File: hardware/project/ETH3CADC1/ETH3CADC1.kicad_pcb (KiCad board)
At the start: 2 copper layers, 73 x 100 mm, 235 parts, among them J1101 Conn_02x10_Odd_Even, J1201 Conn_02x10_Odd_Even, J1301 Conn_02x05_Odd_Even, J401 20021111-00010T4LF, J402 Conn_02x01, J701 Conn_02x10_Odd_Even, J801 Conn_02x02_Odd_Even, J802 Conn_02x04_Odd_Even, Q301 MMBTA55, Q302 BC847, U1001 LM337_SOT223, U1301 AP2127K-1.2, U1302 ICE40UP5K-SG48ITR, U1303 W25Q32JVSS, U201 DG211, U202 DG211B, U203 OPA2192, U204 DG419DY, U205 OPA140, U206 LT5400-100k-100k, U207 LT5400-5k-1k, U208 OPA177, U209 OPA140, U210 LT5400-10k-10k, U211 OPA192, U212 LM311, U301 LT1021-7, U302 LM399H, U303 OPA177, U401 HDC1080, U402 MCP2551-I-SN, U403 STM32H743ZI, U404 PCA9517, U405 24LC08B-E/MS, U501 LAN8742A, U502 LC03-3.3, U503 LC03-3.3, U601 TXB0104PW, U602 ADuM5402, U603 74AC125, U901 MT48LC16M16A2P-6A, X1301 ASAAIG-40.000MHZ, Y401 NX3225GD-8MHZ, Y501 NX5032GA-25.000M-LN-CD-1

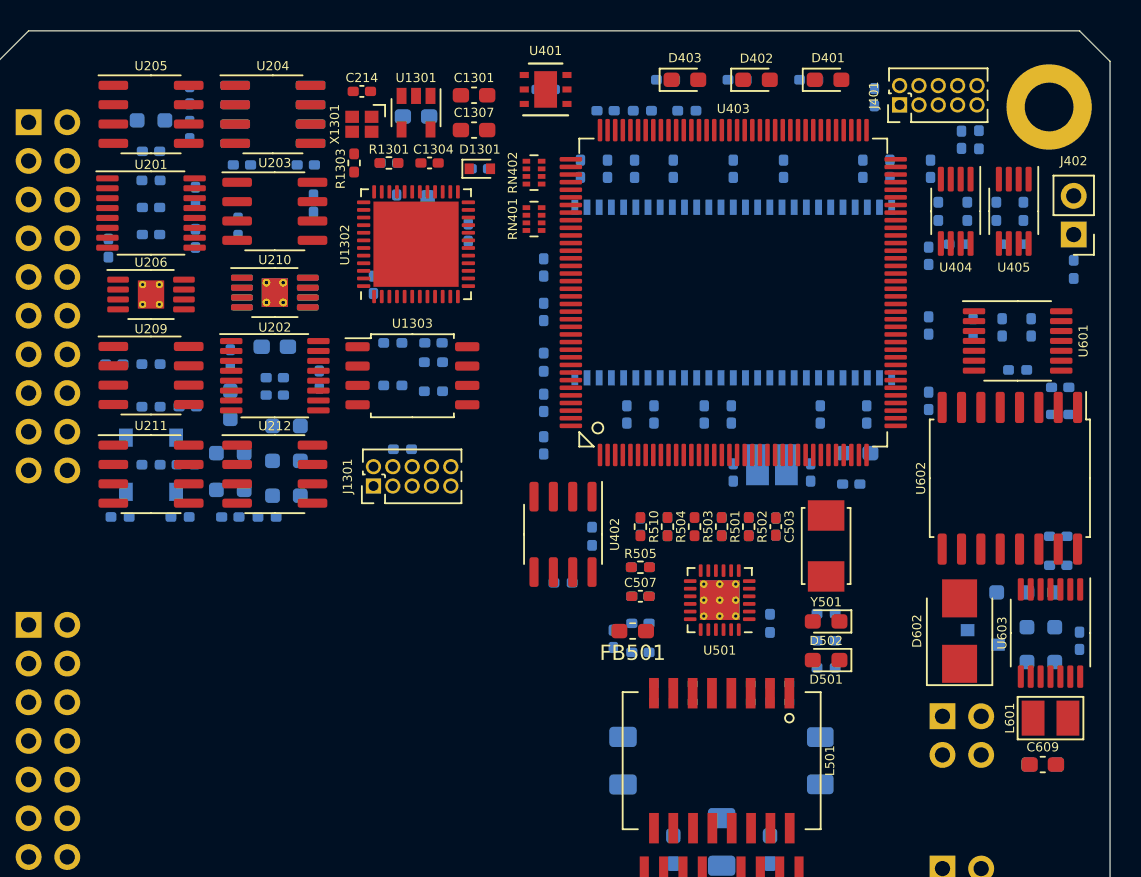
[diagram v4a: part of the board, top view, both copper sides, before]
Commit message: Added SDRAM to the linker file.
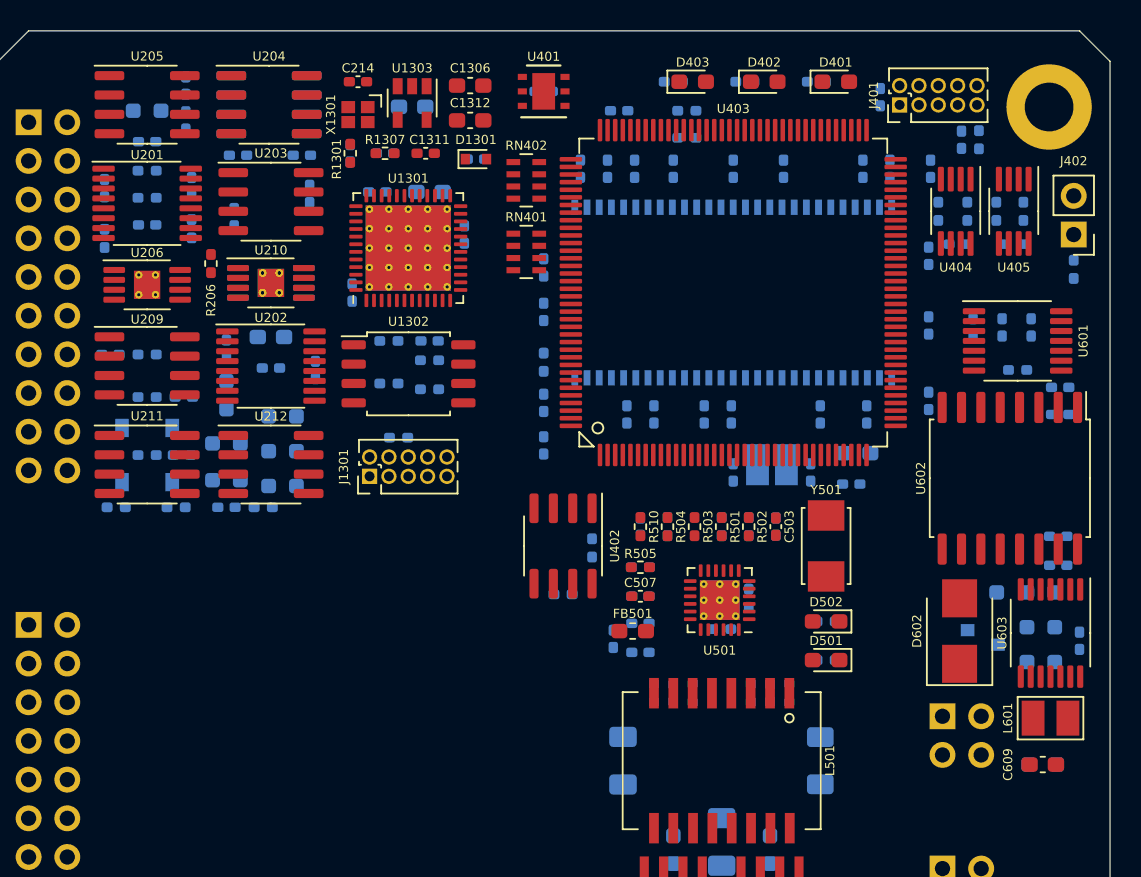
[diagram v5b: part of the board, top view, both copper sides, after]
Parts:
- removed the R203 at (161.0, 59.8)
- added R201: 10k, Resistor_SMD:R_0402_1005Metric_Pad0.72x0.64mm_HandSolder, B.Cu at (160.8, 61.0)
- added R204: 10k, Resistor_SMD:R_0402_1005Metric_Pad0.72x0.64mm_HandSolder, B.Cu at (160.8, 59.2)
- added R206: 10k, Resistor_SMD:R_0402_1005Metric_Pad0.72x0.64mm_HandSolder, F.Cu at (165.0, 65.3)
- D501: value GREEN -> YELLOW
- D502: value YELLOW -> GREEN
- RN401, RN402: footprint Resistor_SMD:R_Array_Concave_4x0402 -> Resistor_SMD:R_Array_Concave_4x0603
- U1301: renamed from U1302; footprint Package_DFN_QFN:QFN-48-1EP_7x7mm_P0.5mm_EP5.6x5.6mm -> Package_DFN_QFN:QFN-48-1EP_7x7mm_P0.5mm_EP5.6x5.6mm_ThermalVias
- moved C218 14.1 mm to (174.1, 58.0), turned to 270 degrees
- moved C219 14.0 mm to (160.8, 62.7)
- moved R511 6.83 mm to (200.3, 87.2), turned to 90 degrees
- moved R402 3.42 mm to (196.2, 57.0), turned to 180 degrees
- moved C210 3.30 mm to (158.0, 60.3), turned to 90 degrees
- moved R512 3.20 mm to (198.5, 89.3), turned to 0 degrees
- moved RN401 2.22 mm to (185.7, 64.5)
- moved C1303 1.49 mm to (174.2, 67.2)
- moved C1302 1.48 mm to (175.9, 60.6), turned to 180 degrees
- moved C1310 1.28 mm to (179.3, 60.6), turned to 0 degrees
- moved R513 1.27 mm to (205.4, 91.3)
- moved C405 0.89 mm to (191.8, 55.2)
- moved R1302 0.80 mm to (177.3, 76.7)
- moved R401 0.76 mm to (188.1, 87.0)
- moved R403 0.76 mm to (190.0, 83.9)
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- renumbered C1308 to C1301, C1309 to C1302, C1310 to C1303, C1311 to C1304, C1312 to C1305, C1301 to C1306, C1302 to C1307, C1303 to C1308, C1305 to C1309, C1306 to C1310, C1304 to C1311, C1307 to C1312, R1303 to R1301, R1305 to R1302, R1302 to R1303, R1306 to R1305, R1307 to R1306, R1301 to R1307, R201 to R202, R202 to R203, R204 to R205, R205 to R207, R206 to R208, R207 to R209, R208 to R210, R209 to R211, R210 to R212, R211 to R213, R212 to R214, R213 to R215, R214 to R216, R215 to R217, R216 to R218, U1303 to U1302, U1301 to U1303
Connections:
- net /ADC 1/FPGA1_MUX_10V renamed /ADC 1/FPGA1_MUX_P10V
- net /ADC 1/VREF1_-7V renamed Net-(U204-Pad8)
- C1301 pad 1: +3V3 -> +3.3VF
- C1302 pad 1: +3V3 -> +3.3VF
- C1303 pad 1: +3V3 -> +3.3VF
- C1304 pad 1: +3V3 -> +3.3VF
- C1305 pad 1: +3V3 -> +3.3VF
- C1306 pad 1: +3V3 -> +3.3VF
- C1309 pad 1: +3V3 -> +3.3VF
- C218 pad 1: +5VF -> +3.3VF
- C218 pad 2: DGNDF -> AGNDF
- C219 pad 1: +5VF -> +3.3VF
- C219 pad 2: DGNDF -> AGNDF
- C220 pad 1: +3.3VP -> +3.3VF
- C301 pad 1: /VREF/VREF_N7V_LPF -> /ADC 1/VREF_N7V_LPF
- C401 pad 1: +3V3 -> +3.3VF
- C402 pad 1: +3V3 -> +3.3VF
- C403 pad 1: +3V3 -> +3.3VF
- C404 pad 1: +3V3 -> +3.3VF
- C405 pad 1: +3V3 -> +3.3VF
- C406 pad 1: +3V3 -> +3.3VF
- C407 pad 1: +3V3 -> +3.3VF
- C408 pad 1: +3V3 -> +3.3VF
- C409 pad 1: +3V3 -> +3.3VF
- C410 pad 1: +3V3 -> +3.3VF
- C411 pad 1: +3V3 -> +3.3VF
- C412 pad 1: +3V3 -> +3.3VF
- C413 pad 1: +3V3 -> +3.3VF
- C417 pad 1: +3V3 -> +3.3VF
- C420 pad 1: +3V3 -> +3.3VF
- C421 pad 1: +3V3 -> +3.3VF
- C422 pad 1: +3V3 -> +3.3VF
- C423 pad 1: +3V3 -> +3.3VF
- C502 pad 1: +3V3 -> +3.3VF
- C505 pad 1: +3V3 -> +3.3VF
- C601 pad 1: +3V3 -> +3.3VF
- C602 pad 1: +3V3 -> +3.3VF
- C901 pad 1: +3V3 -> +3.3VF
- C902 pad 1: +3V3 -> +3.3VF
- C903 pad 1: +3V3 -> +3.3VF
- C904 pad 1: +3V3 -> +3.3VF
- C905 pad 1: +3V3 -> +3.3VF
- C906 pad 1: +3V3 -> +3.3VF
- C907 pad 1: +3V3 -> +3.3VF
- D1301 pad 2: +3V3 -> +3.3VF
- D401 pad 2: +3V3 -> +3.3VF
- D402 pad 2: +3V3 -> +3.3VF
- D403 pad 2: +3V3 -> +3.3VF
- FB401 pad 2: +3V3 -> +3.3VF
- FB501 pad 2: +3V3 -> +3.3VF
- J1101 pad 15: +3V3 -> +3.3VF
- J1101 pad 16: +3V3 -> +3.3VF
- J1201 pad 15: +3V3 -> +3.3VF
- J1201 pad 16: +3V3 -> +3.3VF
- J401 pad 1: +3V3 -> +3.3VF
- J701 pad 15: +3V3 -> +3.3VF
- J701 pad 16: +3V3 -> +3.3VF
- R1302 pad 1: +3V3 -> +3.3VF
- R1303 pad 1: +3V3 -> +3.3VF
- R1304 pad 1: +3V3 -> +3.3VF
- R1305 pad 1: +3V3 -> +3.3VF
- R1306 pad 1: +3V3 -> +3.3VF
- R205 pad 1: Net-(R204-Pad1) -> Net-(R205-Pad1)
- R216 pad 1: +3.3VP -> +3.3VF
- R308 pad 1: /VREF/VREF_N7V_LPF -> /ADC 1/VREF_N7V_LPF
- R309 pad 1: /VREF/VREF_N7V_LPF -> /ADC 1/VREF_N7V_LPF
- R402 pad 1: +3V3 -> +3.3VF
- R404 pad 1: +3V3 -> +3.3VF
- R405 pad 1: +3V3 -> +3.3VF
- R406 pad 1: +3V3 -> +3.3VF
- R407 pad 1: +3V3 -> +3.3VF
- R408 pad 1: +3V3 -> +3.3VF
- R413 pad 1: +3V3 -> +3.3VF
- R414 pad 2: +3V3 -> +3.3VF
- R506 pad 1: +3V3 -> +3.3VF
- R507 pad 1: +3V3 -> +3.3VF
- R508 pad 1: +3V3 -> +3.3VF
- R509 pad 1: +3V3 -> +3.3VF
- R510 pad 1: +3V3 -> +3.3VF
- R601 pad 1: +3V3 -> +3.3VF
- U1301 pad 1: +3V3 -> +3.3VF
- U1301 pad 22: +3V3 -> +3.3VF
- U1301 pad 33: +3V3 -> +3.3VF
- U1301 pad 35: (no net) -> /ADC 1/FPGA1_MUX_N7V
- U1302 pad 8: +3V3 -> +3.3VF
- U1303 pad 1: +3V3 -> +3.3VF
- U1303 pad 3: +3V3 -> +3.3VF
- U201 pad 10: Net-(R204-Pad1) -> Net-(R205-Pad1)
- U201 pad 14: (no net) -> Net-(R204-Pad1)
- U201 pad 15: (no net) -> Net-(R205-Pad1)
- U201 pad 16: Net-(R203-Pad1) (its old number) -> /ADC 1/FPGA1_MUX_N7V
- U201 pad 2: /ADC 1/ADIN1 -> Net-(R201-Pad1)
- U201 pad 3: Net-(R204-Pad1) -> Net-(R205-Pad1)
- U201 pad 6: Net-(R204-Pad1) -> Net-(R205-Pad1)
- U205 pad 2: Net-(U205-Pad2) -> Net-(R206-Pad2)
- U205 pad 3: Net-(R204-Pad1) -> Net-(R205-Pad1)
- U205 pad 6: Net-(U205-Pad2) -> Net-(R206-Pad2)
- U206 pad 8: Net-(U205-Pad2) -> Net-(R206-Pad1)
- U208 pad 3: (no net) -> /ADC 1/VREF_N7V_LPF
- U212 pad 1: DGNDF -> AGNDF
- U212 pad 8: +3.3VP -> +3.3VF
- U401 pad 5: +3V3 -> +3.3VF
- U403 pad 108: +3V3 -> +3.3VF
- U403 pad 121: +3V3 -> +3.3VF
- U403 pad 131: +3V3 -> +3.3VF
- U403 pad 137: (no net) -> /MCU/MODULE_SDA
- U403 pad 139: (no net) -> /MCU/MODULE_SCL
- U403 pad 143: +3V3 -> +3.3VF
- U403 pad 144: +3V3 -> +3.3VF
- U403 pad 17: +3V3 -> +3.3VF
- U403 pad 30: +3V3 -> +3.3VF
- U403 pad 39: +3V3 -> +3.3VF
- U403 pad 52: +3V3 -> +3.3VF
- U403 pad 6: +3V3 -> +3.3VF
- U403 pad 62: +3V3 -> +3.3VF
- U403 pad 72: +3V3 -> +3.3VF
- U403 pad 84: +3V3 -> +3.3VF
- U403 pad 95: +3V3 -> +3.3VF
- U404 pad 1: +3V3 -> +3.3VF
- U404 pad 5: +3V3 -> +3.3VF
- U404 pad 6: /MCU/EEPROM_SCL -> /MCU/MODULE_SCL
- U404 pad 7: /MCU/EEPROM_SDA -> /MCU/MODULE_SDA
- U404 pad 8: +3V3 -> +3.3VF
- U405 pad 8: +3V3 -> +3.3VF
- U501 pad 9: +3V3 -> +3.3VF
- U601 pad 1: +3V3 -> +3.3VF
- U901 pad 1: +3V3 -> +3.3VF
- U901 pad 14: +3V3 -> +3.3VF
- U901 pad 27: +3V3 -> +3.3VF
- U901 pad 3: +3V3 -> +3.3VF
- U901 pad 43: +3V3 -> +3.3VF
- U901 pad 49: +3V3 -> +3.3VF
- U901 pad 9: +3V3 -> +3.3VF
- X1301 pad 4: +3V3 -> +3.3VF
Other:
- copper layers 2 -> 6

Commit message: PCB and software development.
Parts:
- added R219: 0, Resistor_SMD:R_0402_1005Metric_Pad0.72x0.64mm_HandSolder, B.Cu at (158.2, 54.9)
- moved RN402 1.80 mm to (185.4, 61.6)
- moved RN401 1.80 mm to (185.4, 66.3)
- moved C212 1.53 mm to (169.9, 60.8)
- moved C205 1.49 mm to (167.9, 61.7)
- moved C1301 0.89 mm to (182.5, 63.4)
- moved C417 0.40 mm to (187.2, 53.8)
- moved U401 0.40 mm to (187.2, 53.8)
- moved C216 0.25 mm to (170.7, 58.2)
- moved R1304 0.25 mm to (179.3, 73.8)
- moved R1305 0.25 mm to (176.7, 73.4)
- moved R1306 0.25 mm to (179.3, 71.9)
- moved U1302 0.25 mm to (177.9, 72.8)
- moved C1307 0.25 mm to (178.2, 54.7)
- moved C1304 0.25 mm to (179.3, 70.6)
- moved C204 0.25 mm to (167.0, 58.2)
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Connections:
- U1301 pad 19: (no net) -> /FPGA 1/FGPA1_MOSI
- U1301 pad 20: /FPGA 1/FPGA_CLK -> /FPGA 1/FGPA1_MISO
- U1301 pad 21: (no net) -> /FPGA 1/FGPA1_SCLK
- U1301 pad 23: /ADC 1/FGPA1_AD_ID -> /FPGA 1/FGPA1_nSS
- U1301 pad 25: /FPGA 1/FGPA1_AD_VRH -> (no net)
- U1301 pad 26: /ADC 1/FGPA1_AD_IIN -> (no net)
- U1301 pad 27: /ADC 1/FGPA1_AD_IRP -> (no net)
- U1301 pad 28: /ADC 1/FGPA1_AD_IRN -> (no net)
- U1301 pad 31: /FPGA 1/ADC_COMP1 -> (no net)
- U1301 pad 32: /ADC 1/FPGA1_MUX_ADIN -> (no net)
- U1301 pad 34: /ADC 1/FPGA1_MUX_P10V -> (no net)
- U1301 pad 35: /ADC 1/FPGA1_MUX_N7V -> /FPGA 1/FPGA_CLK
- U1301 pad 37: /ADC 1/FPGA1_MUX_GND -> /FPGA 1/FGPA1_AD_VRH
- U1301 pad 38: (no net) -> /ADC 1/FPGA1_MUX_ADIN
- U1301 pad 39: (no net) -> /ADC 1/FPGA1_MUX_N7V
- U1301 pad 40: (no net) -> /ADC 1/FPGA1_MUX_P10V
- U1301 pad 41: (no net) -> /ADC 1/FPGA1_MUX_GND
- U1301 pad 42: (no net) -> /ADC 1/FGPA1_AD_IIN
- U1301 pad 43: (no net) -> /ADC 1/FGPA1_AD_IRN
- U1301 pad 44: /FPGA 1/FGPA1_nSS -> /ADC 1/FGPA1_AD_ID
- U1301 pad 45: (no net) -> /ADC 1/FGPA1_AD_IRP
- U1301 pad 46: /FPGA 1/FGPA1_MISO -> (no net)
- U1301 pad 47: /FPGA 1/FGPA1_MOSI -> /FPGA 1/ADC_COMP1
- U1301 pad 48: /FPGA 1/FGPA1_SCLK -> (no net)
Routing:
- net -14VF: track 0.00 -> 17.7 mm, vias 0 -> 9
- net +18VF: track 0.00 -> 16.4 mm, vias 0 -> 7
- net +3.3VF: track 0.00 -> 12.6 mm, vias 0 -> 8
- net Net-(C215-Pad2): track 0.00 -> 12.2 mm, vias 0 -> 1
- net Net-(C215-Pad1): track 0.00 -> 10.1 mm, vias 0 -> 1
- net Net-(U202-Pad2): track 0.00 -> 6.53 mm
- net Net-(R210-Pad2): track 0.00 -> 5.06 mm, vias 0 -> 1
- net Net-(R216-Pad2): track 0.00 -> 4.57 mm
- net Net-(U203-Pad5): track 0.00 -> 4.53 mm
- net Net-(C209-Pad1): track 0.00 -> 2.98 mm, vias 0 -> 1
- net Net-(C220-Pad2): track 0.00 -> 2.20 mm, vias 0 -> 1
- net Net-(R206-Pad1): track 0.00 -> 2.10 mm
- net Net-(R214-Pad1): track 0.00 -> 2.10 mm, vias 0 -> 1
- net /FPGA 1/ADC_COMP1: track 0.00 -> 1.98 mm, vias 0 -> 1
- net Net-(R208-Pad1): track 0.00 -> 1.94 mm, vias 0 -> 1
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
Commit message: PCB layout
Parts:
- removed RN401, RN402: R_Pack04, Resistor_SMD:R_Array_Concave_4x0603
- added R1308: 10k, Resistor_SMD:R_0402_1005Metric_Pad0.72x0.64mm_HandSolder, B.Cu at (173.1, 69.6)
- added R1309: NC, Resistor_SMD:R_0402_1005Metric_Pad0.72x0.64mm_HandSolder, B.Cu at (174.2, 69.6)
- C424, R413: moved to F.Cu
- moved C402 21.5 mm to (197.4, 56.5), turned to 0 degrees
- moved C416 4.15 mm to (202.7, 75.2), turned to 90 degrees
- moved C415 4.10 mm to (200.8, 75.2), turned to 90 degrees
- moved C905 3.94 mm to (199.3, 59.1)
- moved C401 3.91 mm to (208.3, 75.2), turned to 270 degrees
- moved R404 3.81 mm to (196.3, 59.1), turned to 90 degrees
- moved R402 2.62 mm to (194.6, 59.1), turned to 90 degrees
- moved Q301 2.13 mm to (209.2, 137.7)
- moved R301 2.13 mm to (209.2, 140.6)
- moved R303 2.13 mm to (209.2, 134.7)
- moved R307 2.13 mm to (201.2, 137.7)
- moved U301 2.13 mm to (204.6, 137.7)
- moved C906 1.78 mm to (197.5, 59.1)
- moved C405 1.63 mm to (190.8, 56.5)
- moved C407 1.52 mm to (207.4, 54.4)
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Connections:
- U1301 pad 2: (no net) -> /FPGA 1/CODE1
- U1301 pad 25: (no net) -> /FPGA 1/FPGA1_UART6_TX
- U1301 pad 26: (no net) -> /FPGA 1/FPGA1_UART6_RX
- U1301 pad 3: (no net) -> /FPGA 1/CODE2
- U403 pad 101: (no net) -> Net-(R412-Pad1)
- U403 pad 112: /MCU/MCU_MISO -> /FPGA 1/FGPA1_MISO
- U403 pad 113: /MCU/MCU_MOSI -> /FPGA 1/FGPA1_MOSI
- U403 pad 137: /MCU/MODULE_SDA -> (no net)
- U403 pad 139: /MCU/MODULE_SCL -> (no net)
- U403 pad 40: (no net) -> /MCU/TRIG_IN
- U403 pad 41: (no net) -> /MCU/TRIG_OUT
- U403 pad 42: (no net) -> /MCU/TRIG_EN
- U403 pad 46: Net-(J402-Pad1) -> (no net)
- U403 pad 48: (no net) -> Net-(J402-Pad1)
- U403 pad 69: (no net) -> /MCU/MODULE_SCL
- U403 pad 7: /MCU/TRIG_EN -> (no net)
- U403 pad 70: (no net) -> /MCU/MODULE_SDA
- U403 pad 8: /MCU/TRIG_OUT -> (no net)
- U403 pad 9: /MCU/TRIG_IN -> (no net)
- U403 pad 91: Net-(R412-Pad1) -> (no net)
- U403 pad 96: (no net) -> /FPGA 1/FPGA1_UART6_TX
- U403 pad 97: (no net) -> /FPGA 1/FPGA1_UART6_RX
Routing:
- net (no net): track 0.00 -> 184.4 mm
- net +5V: track 0.00 -> 171.4 mm, vias 0 -> 3
- net /CH1 Connector/I2C_SDA: track 0.00 -> 143.7 mm, vias 0 -> 1
- net /CH1 Connector/I2C_SCL: track 0.00 -> 141.5 mm, vias 0 -> 1
- net +3.3VF: track 12.6 -> 132.2 mm, vias 8 -> 52
- net +18VF: track 16.4 -> 120.5 mm, vias 7 -> 8
- net -18VF: track 0.00 -> 91.4 mm, vias 0 -> 16
- net /CH1 Connector/CANH: track 0.00 -> 69.9 mm, vias 0 -> 1
- net /CH1 Connector/CANL: track 0.00 -> 69.8 mm, vias 0 -> 1
- net /Ethernet/NRST: track 0.00 -> 68.4 mm, vias 0 -> 2
- net AGNDF: track 0.00 -> 41.0 mm, vias 0 -> 19
- net -14VF: track 17.7 -> 52.4 mm, vias 9 -> 20
- net /MCU/CAN_RX: track 0.00 -> 34.4 mm, vias 0 -> 2
- net Net-(R307-Pad1): track 0.00 -> 32.8 mm, vias 0 -> 3
- net /Ethernet/RMII_MDIO: track 0.00 -> 32.7 mm, vias 0 -> 2
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- added copper zone on In2.Cu, net +18VF
- added copper zone on F.Cu, net +3.3VF
- added copper zone on In3.Cu, net +3.3VF
- added copper zone on In2.Cu, net +5V_TRIG
- added copper zone on B.Cu, net -14VF
- added copper zone on F.Cu, net -14VF
- added copper zone on In4.Cu, net -14VF
- added copper zone on B.Cu, net -18VF
- added copper zone on F.Cu, net -18VF
- added copper zone on In3.Cu, net -18VF
- added copper zone on B.Cu, net AGNDF
- added copper zone on F.Cu, net AGNDF
- added copper zone on GND, net AGNDF
- added copper zone on B.Cu, net Earth
- added copper zone on F.Cu, net Earth
- added copper zone on GND, net Earth
- added copper zone on In2.Cu, net Earth
- added copper zone on In3.Cu, net Earth
- added copper zone on In4.Cu, net Earth
- added copper zone on B.Cu, net GND_TRIG
- added copper zone on F.Cu, net GND_TRIG
- added copper zone on GND, net GND_TRIG
- added copper zone on F.Cu, net Net-(C1307-Pad1)
- added copper zone on B.Cu, net Net-(C514-Pad1)
- added copper zone on In2.Cu, net VCCQ
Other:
- outline, holes or cut-outs redrawn
- board text added: "1"
- board text added: "2"
- board text added: "3"
- board text added: "4"
- board text added: "5"
- board text added: "6"
